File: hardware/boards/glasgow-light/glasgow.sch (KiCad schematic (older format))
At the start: 84 parts, among them J1 USB_C_USB2.0, U15 TPD3S014, U36 TLV73312PQDRVR, U5 ICE40UP5K-SG48ITR, U7 GD32VF103, U8 TLV75533PDRVR, Y1 8M

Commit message: start routing FPGA
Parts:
- removed C18, C24, C25, C77, C81: u1, Capacitor_SMD:C_0402_1005Metric, symbol Device:C
- added unit 1 of U5
- C14, C19, C22, C29, C30, C31: footprint Capacitor_SMD:C_0603_1608Metric -> Capacitor_SMD:C_0603_1608Metric_Pad1.08x0.95mm_HandSolder
- C20, C21, C23: footprint Capacitor_SMD:C_0402_1005Metric -> Capacitor_SMD:C_0603_1608Metric_Pad1.08x0.95mm_HandSolder
- R6: footprint Resistor_SMD:R_0603_1608Metric -> Resistor_SMD:R_0603_1608Metric_Pad0.98x0.95mm_HandSolder
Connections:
- net labels added: DA0, DA1, DA2, DA3, DA4, DA5, DA6, DA7, QA1, QA2, QA3, QA4, QA5, QA6, QA7, ~SYNC
- net labels removed: A0, A1, D0, D1, D2, D3, D4, D5, D6, D7, FLAGA, FLAGB, FLAGC, FLAGD, OE, PKTEND, QB7, RD, WR
- wire segments 341 -> 327
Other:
- note removed: "Addr: 0001000"
- moved on the sheet: C14, C19, C20, C21, C22, C23, C29, C30, C31, R6, U5D

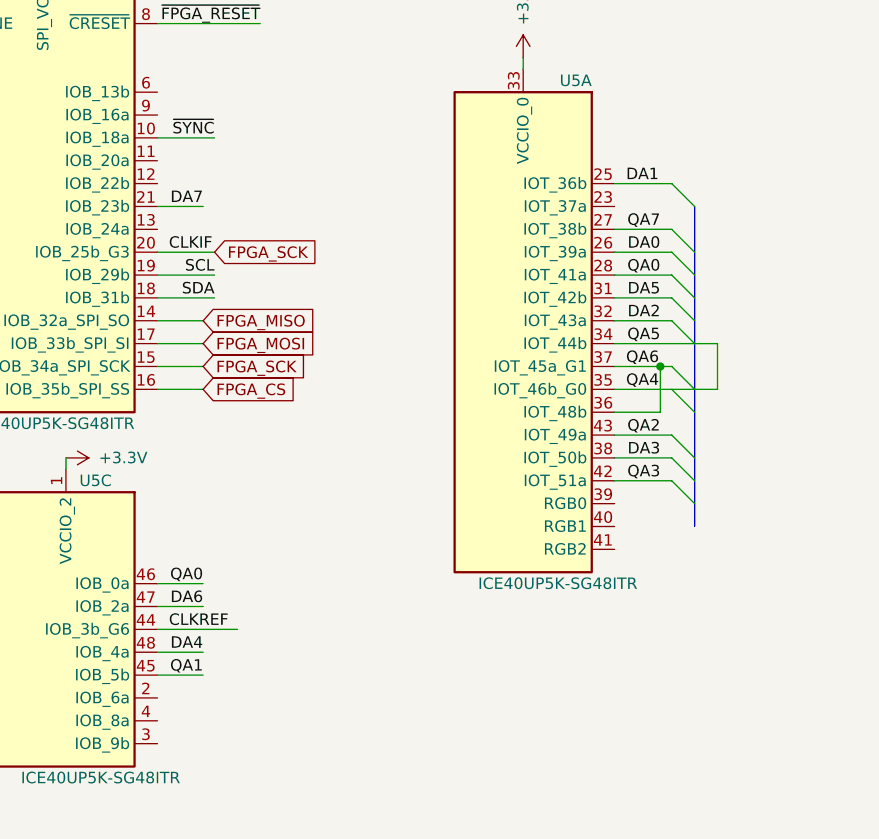
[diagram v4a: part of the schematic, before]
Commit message: right side of FPGA routed
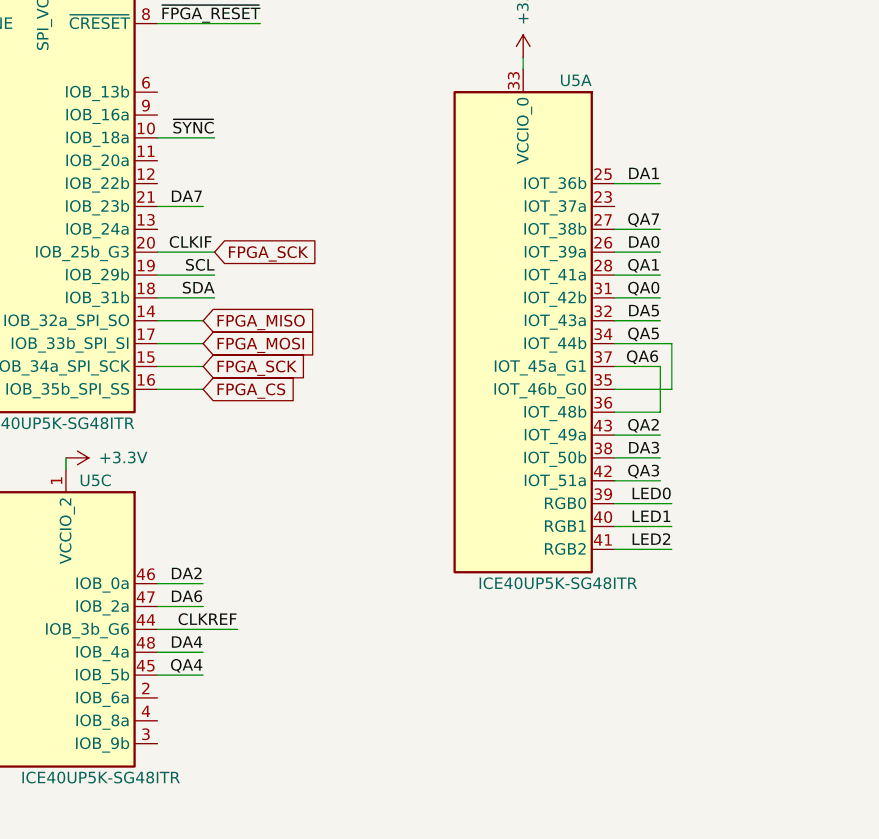
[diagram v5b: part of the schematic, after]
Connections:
- net labels added: LED0, LED1, LED2
- wire segments 327 -> 329
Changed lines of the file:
@@
 Connection ~ 5950 1350
 Connection ~ 5950 950
-Text Label -4950 5000 0    50   ~ 0
+Text Label -4650 5000 2    50   ~ 0
 CLKREF
 $Comp
@@
 Text Label -2800 3350 2    50   ~ 0
 DA0
-Text Label -4800 4800 2    50   ~ 0
-QA0
 Text Label -4750 2850 2    50   ~ 0
 ~SYNC
@@
 Wire Wire Line
 	-5000 4800 -4800 4800
-Text Label -2800 3650 2    50   ~ 0
+Text Label -4800 4800 2    50   ~ 0
 DA2
 Wire Wire Line
 	-4800 3150 -5000 3150
 Wire Wire Line
-	-2750 3850 -2800 3850
-Wire Wire Line
-	-2750 4150 -3000 4150
-Wire Wire Line
-	-2750 4250 -3000 4250
-Wire Wire Line
-	-2750 4350 -3000 4350
-Entry Wire Line
-	-2750 3050 -2650 3150
-Entry Wire Line
-	-2750 3250 -2650 3350
-Entry Wire Line
-	-2750 3350 -2650 3450
-Entry Wire Line
-	-2750 3450 -2650 3550
-Entry Wire Line
-	-2750 3550 -2650 3650
-Entry Wire Line
-	-2750 3650 -2650 3750
-Entry Wire Line
-	-2750 3850 -2650 3950
-Entry Wire Line
-	-2750 3950 -2650 4050
-Entry Wire Line
-	-2750 4150 -2650 4250
-Entry Wire Line
-	-2750 4250 -2650 4350
-Entry Wire Line
-	-2750 4350 -2650 4450
+	-2800 4150 -3000 4150
+Wire Wire Line
+	-2800 4250 -3000 4250
+Wire Wire Line
+	-2800 4350 -3000 4350
 $Comp
 L power:+3.3V #PWR0113
@@
 Text Label -2950 3850 0    50   ~ 0
 QA6
-Text Label -2950 3950 0    50   ~ 0
+Text Label -4800 5200 2    50   ~ 0
 QA4
 Text Label -2800 4350 2    50   ~ 0
@@
 Text Label -2800 4150 2    50   ~ 0
 QA2
-Text Label -4800 5200 2    50   ~ 0
+Text Label -2800 3450 2    50   ~ 0
 QA1
 Wire Wire Line
 	-3400 2550 -3400 2500
-Text Label -2950 3050 0    50   ~ 0
+Text Label -2800 3050 2    50   ~ 0
 DA1
 Text Label -2800 4250 2    50   ~ 0
@@
 Text Label -4800 5100 2    50   ~ 0
 DA4
-Text Label -2800 3550 2    50   ~ 0
+Text Label -2800 3650 2    50   ~ 0
 DA5
 Text Label -4800 4900 2    50   ~ 0
@@
 DA7
 Wire Wire Line
-	-3000 3050 -2750 3050
-Wire Wire Line
-	-3000 3250 -2750 3250
-Wire Wire Line
-	-3000 3350 -2750 3350
-Wire Wire Line
-	-3000 3450 -2750 3450
-Wire Wire Line
-	-3000 3550 -2750 3550
-Wire Wire Line
-	-3000 3650 -2750 3650
+	-3000 3050 -2800 3050
+Wire Wire Line
+	-3000 3250 -2800 3250
+Wire Wire Line
+	-3000 3350 -2800 3350
+Wire Wire Line
+	-3000 3450 -2800 3450
+Wire Wire Line
+	-3000 3550 -2800 3550
+Wire Wire Line
+	-3000 3650 -2800 3650
 $Comp
 L FPGA_Lattice:ICE40UP5K-SG48ITR U5
@@
 Wire Wire Line
 	-2800 4050 -3000 4050
-Connection ~ -2800 3850
 Wire Wire Line
 	-3000 3850 -2800 3850
 Wire Wire Line
-	-2550 3950 -2550 3750
+	-2750 3950 -2750 3750
 Wire Wire Line
 	-4750 2850 -5000 2850
@@
 Wire Wire Line
 	9900 3000 9700 3000
-Wire Wire Line
-	-3000 3750 -2550 3750
-Wire Wire Line
-	-3000 3950 -2550 3950
-Wire Bus Line
-	-2650 3150 -2650 4550
-Text Label -2800 3450 2    50   ~ 0
+Text Label -2800 3550 2    50   ~ 0
 QA0
+Wire Wire Line
+	-3000 4450 -2750 4450
+Wire Wire Line
+	-3000 4550 -2750 4550
+Wire Wire Line
+	-3000 4650 -2750 4650
+Wire Wire Line
+	-3000 3750 -2750 3750
+Wire Wire Line
+	-3000 3950 -2750 3950
+Text Label -2750 4450 2    50   ~ 0
+LED0
+Text Label -2750 4550 2    50   ~ 0
+LED1
+Text Label -2750 4650 2    50   ~ 0
+LED2
 $EndSCHEMATC

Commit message: continue routing around FPGA
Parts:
- added D14, D15, D5: YEL, LED_SMD:LED_0603_1608Metric, symbol Device:LED
- added R26, R27, R28: 0, Resistor_SMD:R_0402_1005Metric, symbol Device:R
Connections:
- wire segments 329 -> 343
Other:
- moved on the sheet: D4, R15
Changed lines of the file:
@@
 L Device:LED D4
 U 1 1 5B097E38
-P 9800 1500
-F 0 "D4" H 9500 1500 50  0000 C CNN
-F 1 "YEL" H 9350 1500 50  0000 C CNN
-F 2 "LED_SMD:LED_0603_1608Metric" H 9800 1500 50  0001 C CNN
-F 3 "https://www.mouser.com/datasheet/2/445/150060YS75000-368983.pdf" H 9800 1500 50  0001 C CNN
-F 4 "Wurth Electronics" H -450 0   50  0001 C CNN "Mfg"
-F 5 "150060YS75000" H -450 0   50  0001 C CNN "MPN"
-F 6 "led-0603-yel" H 9800 1500 50  0001 C CNN "1b2-bom-key"
-	1    9800 1500
+P 9800 1100
+F 0 "D4" H 9500 1100 50  0000 C CNN
+F 1 "YEL" H 9350 1100 50  0000 C CNN
+F 2 "LED_SMD:LED_0603_1608Metric" H 9800 1100 50  0001 C CNN
+F 3 "https://www.mouser.com/datasheet/2/445/150060YS75000-368983.pdf" H 9800 1100 50  0001 C CNN
+F 4 "Wurth Electronics" H -450 -400 50  0001 C CNN "Mfg"
+F 5 "150060YS75000" H -450 -400 50  0001 C CNN "MPN"
+F 6 "led-0603-yel" H 9800 1100 50  0001 C CNN "1b2-bom-key"
+	1    9800 1100
 	-1   0    0    1
 $EndComp
@@
 	10000 900  9950 900
 Wire Wire Line
-	10000 1500 9950 1500
+	10000 1100 9950 1100
 $Comp
 L Device:R R12
@@
 $EndComp
 Wire Wire Line
-	8900 1500 9300 1500
-Text Label 8900 1500 0    50   ~ 0
+	8900 1100 9300 1100
+Text Label 8900 1100 0    50   ~ 0
 LED_ACT
 Wire Wire Line
@@
 L Device:R R15
 U 1 1 5B2E1435
-P 9450 1500
-F 0 "R15" V 9350 1500 50  0000 C CNN
-F 1 "2k2" V 9450 1500 50  0000 C CNN
-F 2 "Resistor_SMD:R_0402_1005Metric" V 9380 1500 50  0001 C CNN
-F 3 "https://www.mouser.com/datasheet/2/447/PYu-RC_Group_51_RoHS_L_10-1527934.pdf" H 9450 1500 50  0001 C CNN
-F 4 "Yageo" H -450 0   50  0001 C CNN "Mfg"
-F 5 "RC0402FR-132K2L" H -450 0   50  0001 C CNN "MPN"
-F 6 "res-0402-2k2" H 9450 1500 50  0001 C CNN "1b2-bom-key"
-	1    9450 1500
+P 9450 1100
+F 0 "R15" V 9350 1100 50  0000 C CNN
+F 1 "2k2" V 9450 1100 50  0000 C CNN
+F 2 "Resistor_SMD:R_0402_1005Metric" V 9380 1100 50  0001 C CNN
+F 3 "https://www.mouser.com/datasheet/2/447/PYu-RC_Group_51_RoHS_L_10-1527934.pdf" H 9450 1100 50  0001 C CNN
+F 4 "Yageo" H -450 -400 50  0001 C CNN "Mfg"
+F 5 "RC0402FR-132K2L" H -450 -400 50  0001 C CNN "MPN"
+F 6 "res-0402-2k2" H 9450 1100 50  0001 C CNN "1b2-bom-key"
+	1    9450 1100
 	0    -1   1    0
 $EndComp
 Wire Wire Line
-	9650 1500 9600 1500
-Connection ~ 10000 1500
+	9650 1100 9600 1100
 Text Notes 10600 4700 0    50   ~ 0
 500 mA @ 3V3
@@
 L power:GND #PWR0120
 U 1 1 5B138DA0
-P 10000 1750
-F 0 "#PWR0120" H 10000 1500 50  0001 C CNN
-F 1 "GND" H 10005 1577 50  0000 C CNN
-F 2 "" H 10000 1750 50  0001 C CNN
-F 3 "" H 10000 1750 50  0001 C CNN
-	1    10000 1750
-	1    0    0    -1
-$EndComp
-Wire Wire Line
-	10000 1500 10000 1750
-Wire Wire Line
-	10000 900  10000 1500
+P 10000 1150
+F 0 "#PWR0120" H 10000 900 50  0001 C CNN
+F 1 "GND" H 10005 977 50  0000 C CNN
+F 2 "" H 10000 1150 50  0001 C CNN
+F 3 "" H 10000 1150 50  0001 C CNN
+	1    10000 1150
+	1    0    0    -1
+$EndComp
+Wire Wire Line
+	10000 900  10000 1100
 Wire Wire Line
 	2300 3350 2300 3500
@@
 Wire Wire Line
 	-4800 3950 -5000 3950
-Text Label -4750 3550 2    50   ~ 0
-SDA
-Text Label -4750 3450 2    50   ~ 0
-SCL
 Wire Wire Line
 	-4750 3550 -5000 3550
@@
 Text Label -2750 4450 2    50   ~ 0
 LED0
+Text Label -2750 4650 2    50   ~ 0
+LED1
 Text Label -2750 4550 2    50   ~ 0
+LED2
+Connection ~ 10000 1100
+Wire Wire Line
+	10000 1100 10000 1150
+$Comp
+L Device:LED D5
+U 1 1 60A57A73
+P 9450 1500
+F 0 "D5" H 9150 1500 50  0000 C CNN
+F 1 "YEL" H 9000 1500 50  0000 C CNN
+F 2 "LED_SMD:LED_0603_1608Metric" H 9450 1500 50  0001 C CNN
+F 3 "https://www.mouser.com/datasheet/2/445/150060YS75000-368983.pdf" H 9450 1500 50  0001 C CNN
+F 4 "Wurth Electronics" H -800 0   50  0001 C CNN "Mfg"
+F 5 "150060YS75000" H -800 0   50  0001 C CNN "MPN"
+F 6 "led-0603-yel" H 9450 1500 50  0001 C CNN "1b2-bom-key"
+	1    9450 1500
+	-1   0    0    1
+$EndComp
+$Comp
+L Device:LED D14
+U 1 1 60A58470
+P 9450 1700
+F 0 "D14" H 9150 1700 50  0000 C CNN
+F 1 "YEL" H 9000 1700 50  0000 C CNN
+F 2 "LED_SMD:LED_0603_1608Metric" H 9450 1700 50  0001 C CNN
+F 3 "https://www.mouser.com/datasheet/2/445/150060YS75000-368983.pdf" H 9450 1700 50  0001 C CNN
+F 4 "Wurth Electronics" H -800 200 50  0001 C CNN "Mfg"
+F 5 "150060YS75000" H -800 200 50  0001 C CNN "MPN"
+F 6 "led-0603-yel" H 9450 1700 50  0001 C CNN "1b2-bom-key"
+	1    9450 1700
+	-1   0    0    1
+$EndComp
+$Comp
+L Device:LED D15
+U 1 1 60A58B7D
+P 9450 1900
+F 0 "D15" H 9150 1900 50  0000 C CNN
+F 1 "YEL" H 9000 1900 50  0000 C CNN
+F 2 "LED_SMD:LED_0603_1608Metric" H 9450 1900 50  0001 C CNN
+F 3 "https://www.mouser.com/datasheet/2/445/150060YS75000-368983.pdf" H 9450 1900 50  0001 C CNN
+F 4 "Wurth Electronics" H -800 400 50  0001 C CNN "Mfg"
+F 5 "150060YS75000" H -800 400 50  0001 C CNN "MPN"
+F 6 "led-0603-yel" H 9450 1900 50  0001 C CNN "1b2-bom-key"
+	1    9450 1900
+	-1   0    0    1
+$EndComp
+$Comp
+L power:+3.3V #PWR0102
+U 1 1 60A5E017
+P 9200 1700
+F 0 "#PWR0102" H 9200 1550 50  0001 C CNN
+F 1 "+3.3V" V 9200 1950 50  0000 C CNN
+F 2 "" H 9200 1700 50  0001 C CNN
+F 3 "" H 9200 1700 50  0001 C CNN
+	1    9200 1700
+	0    -1   -1   0
+$EndComp
+Wire Wire Line
+	9200 1700 9250 1700
+Wire Wire Line
+	9250 1700 9250 1500
+Wire Wire Line
+	9250 1500 9300 1500
+Connection ~ 9250 1700
+Wire Wire Line
+	9250 1700 9300 1700
+Wire Wire Line
+	9250 1700 9250 1900
+Wire Wire Line
+	9250 1900 9300 1900
+Wire Wire Line
+	9600 1900 10000 1900
+Wire Wire Line
+	9600 1700 10000 1700
+Wire Wire Line
+	9600 1500 10000 1500
+Wire Wire Line
+	10300 1500 10500 1500
+Wire Wire Line
+	10300 1700 10500 1700
+Wire Wire Line
+	10300 1900 10500 1900
+Text Label 10500 1500 2    50   ~ 0
+LED0
+Text Label 10500 1700 2    50   ~ 0
 LED1
-Text Label -2750 4650 2    50   ~ 0
+Text Label 10500 1900 2    50   ~ 0
 LED2
+$Comp
+L Device:R R28
+U 1 1 60A5FEBF
+P 10150 1900
+F 0 "R28" V 10050 1900 50  0000 C CNN
+F 1 "0" V 10150 1900 50  0000 C CNN
+F 2 "Resistor_SMD:R_0402_1005Metric" V 10080 1900 50  0001 C CNN
+F 3 "https://www.mouser.com/datasheet/2/447/PYu-RC_Group_51_RoHS_L_10-1527934.pdf" H 10150 1900 50  0001 C CNN
+F 4 "Yageo" H 250 400 50  0001 C CNN "Mfg"
+F 5 "RC0402FR-132K2L" H 250 400 50  0001 C CNN "MPN"
+F 6 "res-0402-2k2" H 10150 1900 50  0001 C CNN "1b2-bom-key"
+	1    10150 1900
+	0    -1   1    0
+$EndComp
+$Comp
+L Device:R R27
+U 1 1 60A5F89E
+P 10150 1700
+F 0 "R27" V 10050 1700 50  0000 C CNN
+F 1 "0" V 10150 1700 50  0000 C CNN
+F 2 "Resistor_SMD:R_0402_1005Metric" V 10080 1700 50  0001 C CNN
+F 3 "https://www.mouser.com/datasheet/2/447/PYu-RC_Group_51_RoHS_L_10-1527934.pdf" H 10150 1700 50  0001 C CNN
+F 4 "Yageo" H 250 200 50  0001 C CNN "Mfg"
+F 5 "RC0402FR-132K2L" H 250 200 50  0001 C CNN "MPN"
+F 6 "res-0402-2k2" H 10150 1700 50  0001 C CNN "1b2-bom-key"
+	1    10150 1700
+	0    -1   1    0
+$EndComp
+$Comp
+L Device:R R26
+U 1 1 60A5E6F8
+P 10150 1500
+F 0 "R26" V 10050 1500 50  0000 C CNN
+F 1 "0" V 10150 1500 50  0000 C CNN
+F 2 "Resistor_SMD:R_0402_1005Metric" V 10080 1500 50  0001 C CNN
+F 3 "https://www.mouser.com/datasheet/2/447/PYu-RC_Group_51_RoHS_L_10-1527934.pdf" H 10150 1500 50  0001 C CNN
+F 4 "Yageo" H 250 0   50  0001 C CNN "Mfg"
+F 5 "RC0402FR-132K2L" H 250 0   50  0001 C CNN "MPN"
+F 6 "res-0402-2k2" H 10150 1500 50  0001 C CNN "1b2-bom-key"
+	1    10150 1500
+	0    -1   1    0
+$EndComp
+Text Label -4800 5300 2    50   ~ 0
+SCL
+Text Label -4800 5500 2    50   ~ 0
+SDA
+Wire Wire Line
+	-4800 5500 -5000 5500
+Wire Wire Line
+	-5000 5300 -4800 5300
 $EndSCHEMATC

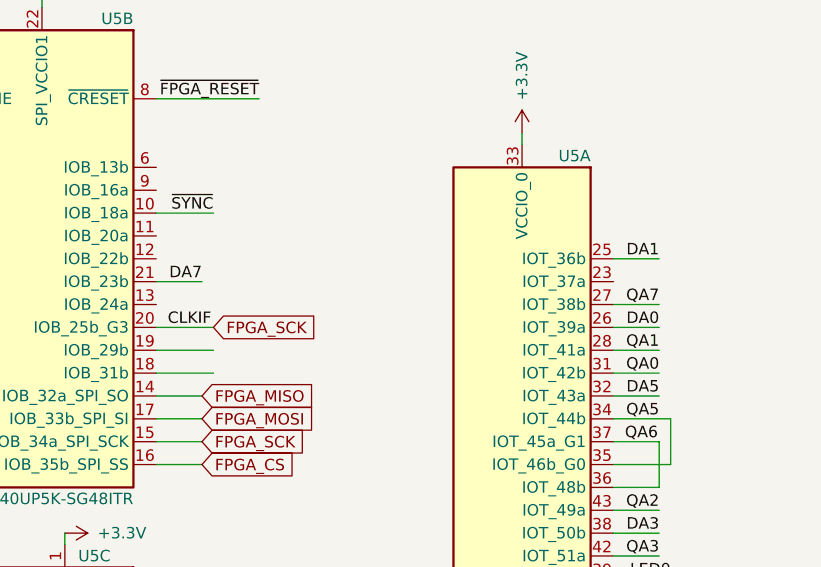
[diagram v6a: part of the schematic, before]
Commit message: swap some of the DAx pins, again
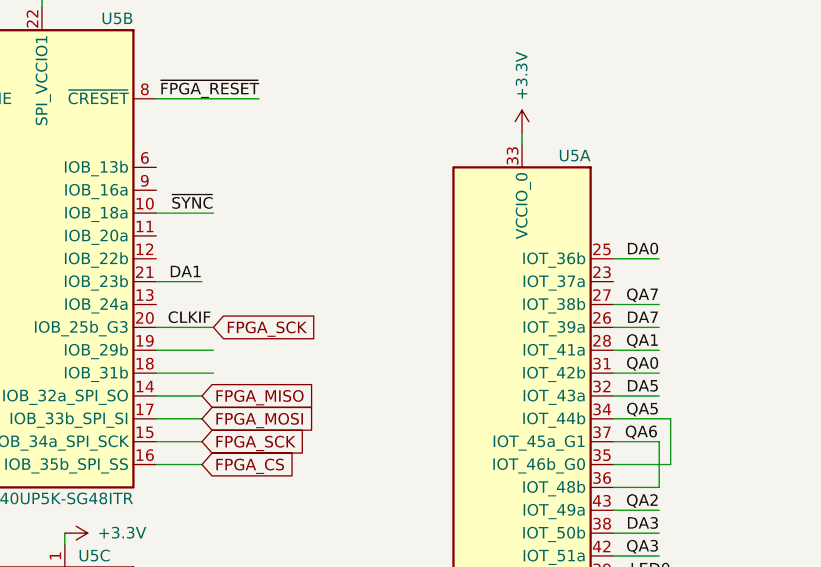
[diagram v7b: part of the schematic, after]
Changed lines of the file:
@@
 Wire Wire Line
 	-5000 3450 -4750 3450
-Text Label -2800 3350 2    50   ~ 0
+Text Label -2800 3050 2    50   ~ 0
 DA0
 Text Label -4750 2850 2    50   ~ 0
@@
 Wire Wire Line
 	-3400 2550 -3400 2500
-Text Label -2800 3050 2    50   ~ 0
+Text Label -4800 3150 2    50   ~ 0
 DA1
 Text Label -2800 4250 2    50   ~ 0
@@
 Text Label -4800 4900 2    50   ~ 0
 DA6
-Text Label -4800 3150 2    50   ~ 0
+Text Label -2800 3350 2    50   ~ 0
 DA7
 Wire Wire Line

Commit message: something
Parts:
- R9: value 15k -> 10k
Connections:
- net labels removed: FPGA_JTAG1, FPGA_JTAG2, FPGA_JTAG3, FPGA_JTAG4, FPGA_JTAG5
- wire segments 343 -> 340
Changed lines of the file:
@@
 P 3000 -2600
 F 0 "R9" V 2900 -2600 50  0000 C CNN
-F 1 "15k" V 3000 -2600 50  0000 C CNN
+F 1 "10k" V 3000 -2600 50  0000 C CNN
 F 2 "Resistor_SMD:R_0402_1005Metric" V 2930 -2600 50  0001 C CNN
 F 3 "https://www.mouser.com/datasheet/2/447/PYu-RC_Group_51_RoHS_L_10-1527934.pdf" H 3000 -2600 50  0001 C CNN
@@
 Text GLabel -400 -2650 2    50   Input ~ 0
 FPGA_MOSI
-Text Label -150 -2500 0    50   ~ 0
+Text Label -200 -2200 2    50   ~ 0
 LED_ACT
 Wire Wire Line
@@
 	4300 -5550 4400 -5550
 Wire Wire Line
-	4300 -4800 4600 -4800
-Wire Wire Line
-	4300 -4650 4600 -4650
-Wire Wire Line
-	4300 -4500 4600 -4500
-Wire Wire Line
-	4300 -4200 4600 -4200
-Wire Wire Line
-	4300 -4050 4600 -4050
-Text Label 4350 -4800 0    50   ~ 0
-FPGA_JTAG1
-Text Label 4350 -4650 0    50   ~ 0
-FPGA_JTAG2
-Text Label 4350 -4500 0    50   ~ 0
-FPGA_JTAG3
-Text Label 4350 -4200 0    50   ~ 0
-FPGA_JTAG4
-Text Label 4350 -4050 0    50   ~ 0
-FPGA_JTAG5
+	4300 -4800 4800 -4800
 Text Notes 50   -2900 0    50   ~ 0
 CLKIF
-Text Label -500 -2200 0    50   ~ 0
+Text Label 150  -2500 2    50   ~ 0
 CLKREF
 Wire Wire Line
@@
 Wire Wire Line
 	-5000 5300 -4800 5300
+Wire Wire Line
+	4300 -4650 4800 -4650
+Text Label 4800 -4800 2    50   ~ 0
+~FPGA_RESET
+Text Label 4800 -4650 2    50   ~ 0
+FPGA_DONE
 $EndSCHEMATC
